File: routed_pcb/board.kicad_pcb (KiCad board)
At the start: 2 copper layers, 100 x 100 mm, 31 parts

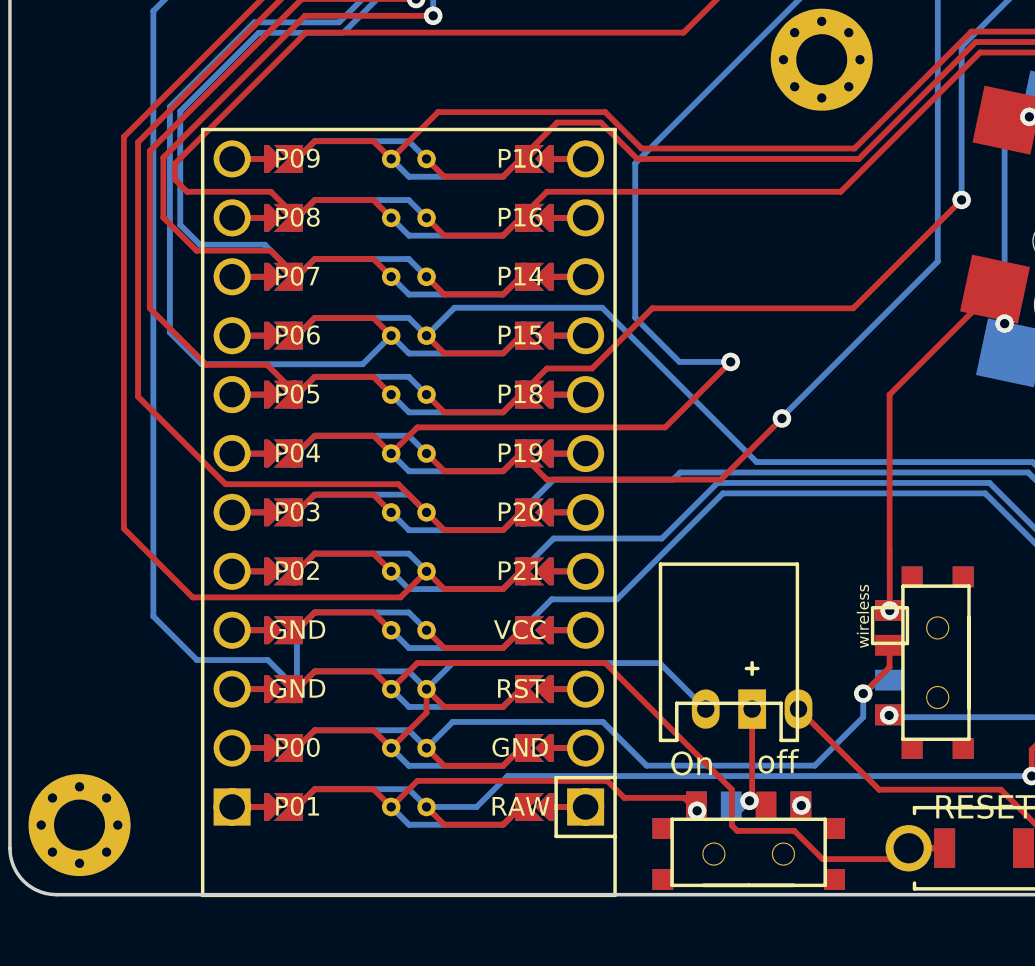
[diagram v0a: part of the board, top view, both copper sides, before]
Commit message: moved text on pro micro
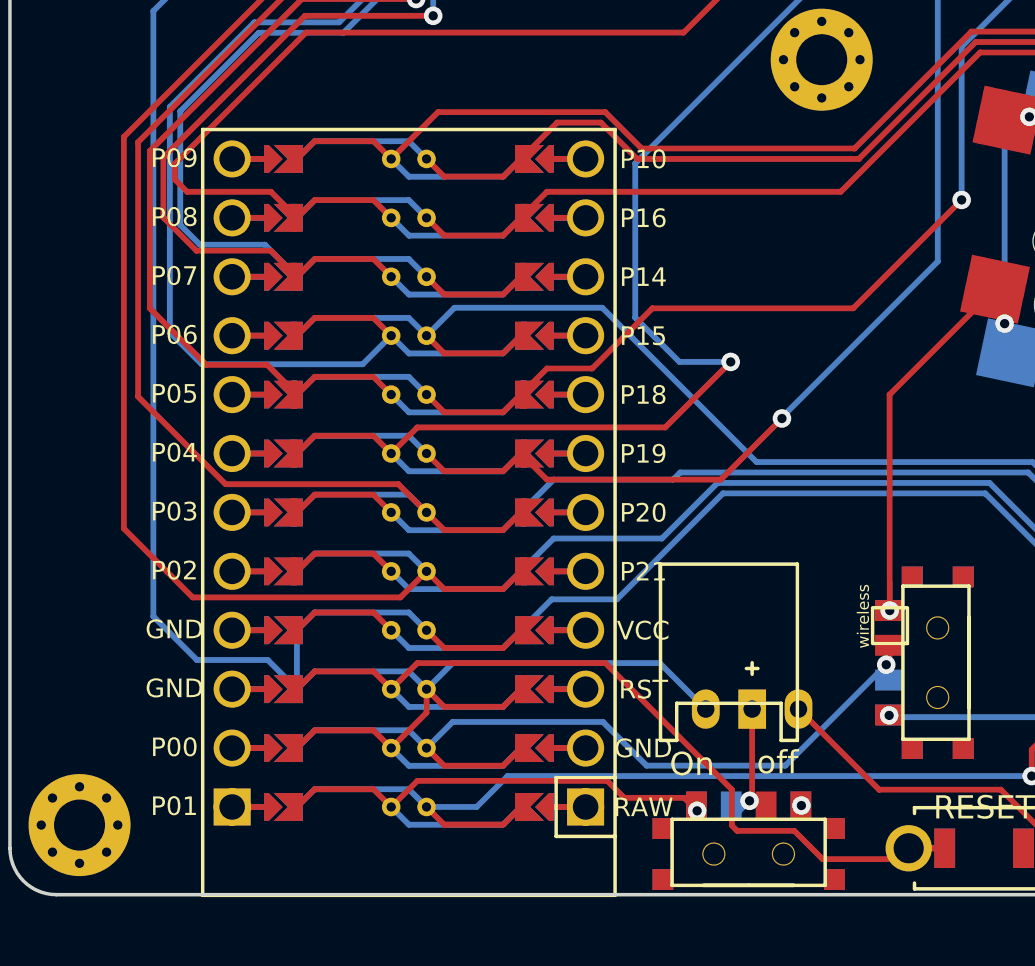
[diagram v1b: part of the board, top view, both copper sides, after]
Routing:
- net /P0: track 25.9 -> 24.5 mm
